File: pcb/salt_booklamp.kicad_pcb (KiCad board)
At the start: 2 copper layers, 45.1 x 45.1 mm, 28 parts, among them J1 USB-C31-S-RA-CS1E-BK-T/R, P1 PIC-TC2050-IDC, U1 PIC16F15213-I/SN, U2 BQ21040DBVR, U3 TPS61158DRVR

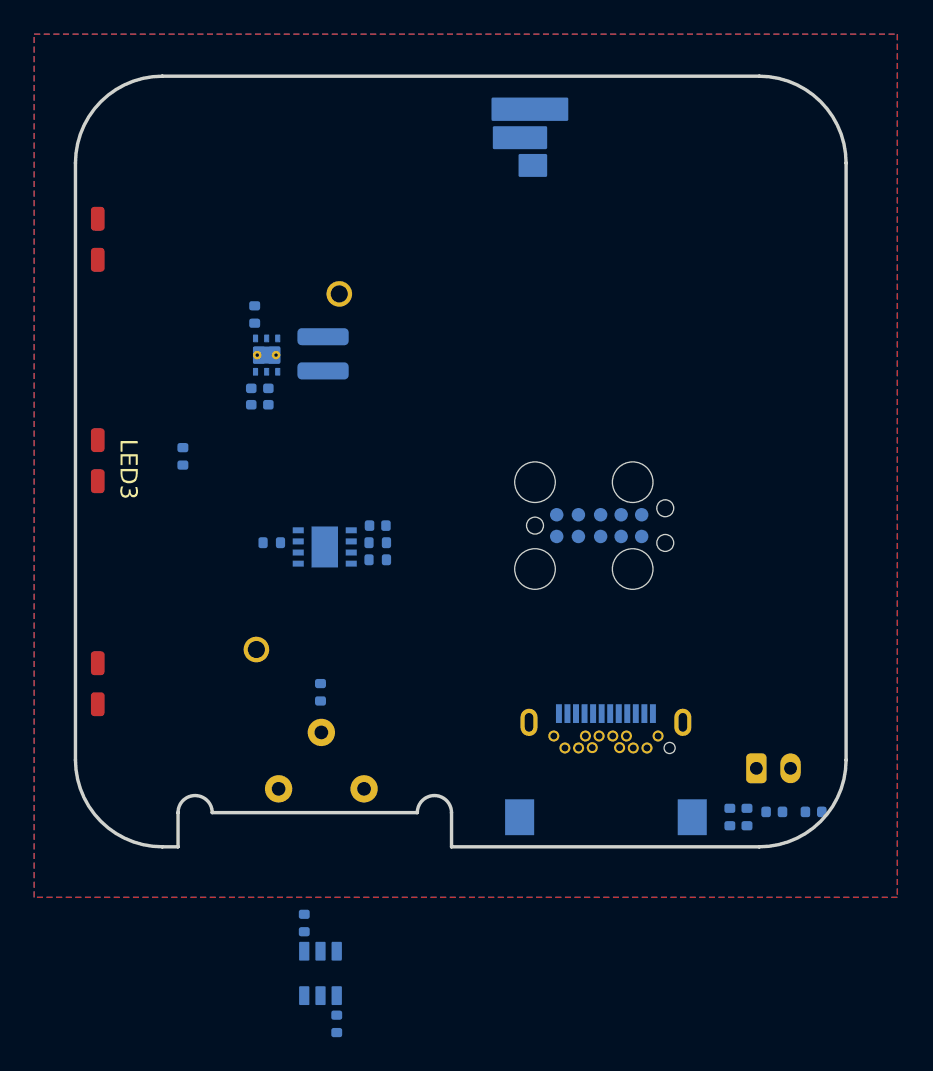
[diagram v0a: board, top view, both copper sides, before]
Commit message: placement work - may need smaller battery connector
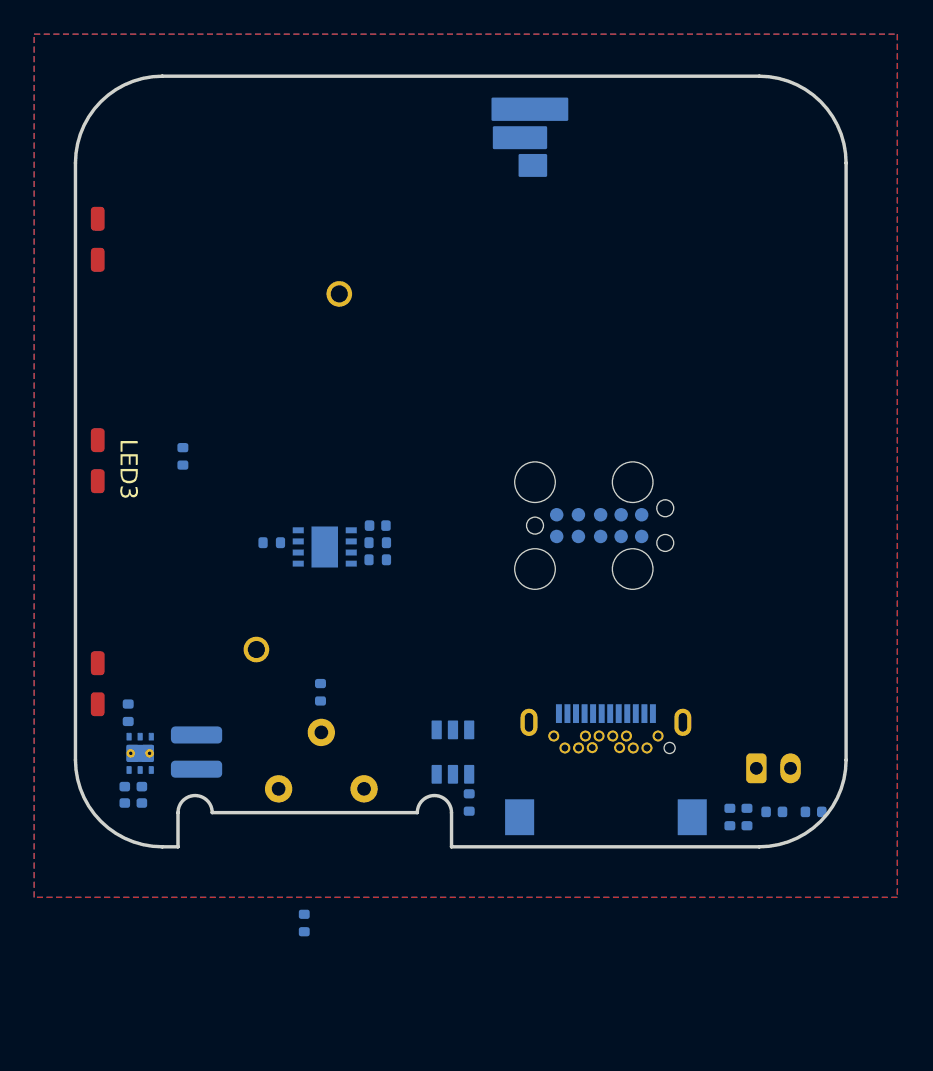
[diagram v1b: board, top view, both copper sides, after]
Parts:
- moved C4 24.4 mm to (204.6, 148.5)
- moved C5 24.4 mm to (205.6, 148.5)
- moved L1 24.4 mm to (208.8, 146.0)
- moved U3 24.4 mm to (205.5, 146.1)
- moved R2 24.4 mm to (204.8, 143.7)
- moved R6 15.1 mm to (224.7, 149.0)
- moved U2 15.1 mm to (223.8, 146.0)
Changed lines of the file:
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@@
 	(footprint "Resistor_SMD:R_0402_1005Metric"
 		(layer "B.Cu")
-		(at 212.182 120.432 -90)
+		(at 204.782 143.732 -90)
 		(descr "Resistor SMD 0402 (1005 Metric), square (rectangular) end terminal, IPC_7351 nominal, (Body size source: IPC-SM-782 page 72, https://www.pcb-3d.com/wordpress/wp-content/uploads/ipc-sm-782a_amendment_1_and_2.pdf), generated with kicad-footprint-generator")
 		(tags "resistor")
@@
 	(footprint "salt_booklamp_footprints:6-WDFN - TPS61158DRVR"
 		(layer "B.Cu")
-		(at 212.882 122.807 90)
+		(at 205.482 146.107 90)
 		(property "Reference" "U3"
 			(at 0 2.1 270)
@@
 	(footprint "salt_booklamp_footprints:BQ21040DBVR"
 		(layer "B.Cu")
-		(at 216.032 158.982)
+		(at 223.782 146.032)
 		(property "Reference" "U2"
 			(at 1.5 3 270)
@@
 	(footprint "Resistor_SMD:R_0402_1005Metric"
 		(layer "B.Cu")
-		(at 216.982 161.932 -90)
+		(at 224.732 148.982 -90)
 		(descr "Resistor SMD 0402 (1005 Metric), square (rectangular) end terminal, IPC_7351 nominal, (Body size source: IPC-SM-782 page 72, https://www.pcb-3d.com/wordpress/wp-content/uploads/ipc-sm-782a_amendment_1_and_2.pdf), generated with kicad-footprint-generator")
 		(tags "resistor")
@@
 	(footprint "salt_booklamp_footprints:ind_VLS3012CX"
 		(layer "B.Cu")
-		(at 216.182 122.732 90)
+		(at 208.782 146.032 90)
 		(property "Reference" "L1"
 			(at 0.2 2.4 270)
@@
 	(footprint "Capacitor_SMD:C_0402_1005Metric"
 		(layer "B.Cu")
-		(at 211.982 125.232 -90)
+		(at 204.582 148.532 -90)
 		(descr "Capacitor SMD 0402 (1005 Metric), square (rectangular) end terminal, IPC_7351 nominal, (Body size source: IPC-SM-782 page 76, https://www.pcb-3d.com/wordpress/wp-content/uploads/ipc-sm-782a_amendment_1_and_2.pdf), generated with kicad-footprint-generator")
 		(tags "capacitor")
@@
 	(footprint "Capacitor_SMD:C_0402_1005Metric"
 		(layer "B.Cu")
-		(at 212.982 125.232 -90)
+		(at 205.582 148.532 -90)
 		(descr "Capacitor SMD 0402 (1005 Metric), square (rectangular) end terminal, IPC_7351 nominal, (Body size source: IPC-SM-782 page 76, https://www.pcb-3d.com/wordpress/wp-content/uploads/ipc-sm-782a_amendment_1_and_2.pdf), generated with kicad-footprint-generator")
 		(tags "capacitor")

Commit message: initial placement for mechanical design -> redesign light guide for 3 LEDs, improve enclosure fit of PCB etc., evaluate battery connector
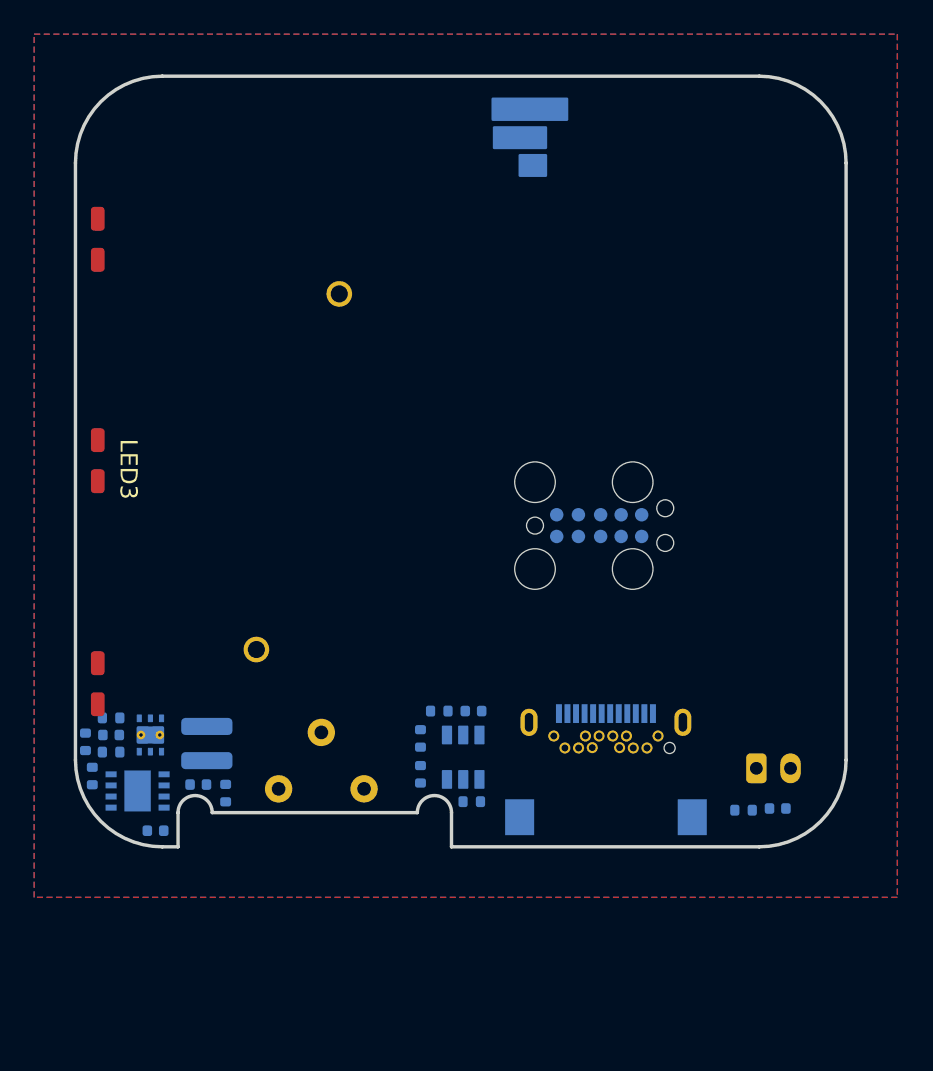
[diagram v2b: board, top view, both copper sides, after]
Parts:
- moved C3 22.1 mm to (206.4, 150.6)
- moved R3 21.6 mm to (202.7, 147.4), turned to 90 degrees
- moved R4 19.2 mm to (203.8, 146.0), turned to 180 degrees
- moved R10 18.7 mm to (221.9, 145.2)
- moved C1 18.6 mm to (225.0, 143.6)
- moved U1 18.0 mm to (205.3, 148.3), turned to 0 degrees
- moved R8 17.6 mm to (202.3, 145.4)
- moved R5 14.9 mm to (210.5, 148.4), turned to 90 degrees
- moved R1 14.7 mm to (223.0, 143.6), turned to 0 degrees
- moved R7 7.57 mm to (221.9, 147.3)
- moved C4 3.59 mm to (203.8, 145.0), turned to 180 degrees
- moved C5 3.35 mm to (208.9, 147.9), turned to 180 degrees
- moved C2 2.11 mm to (242.8, 149.3)
- moved U3 1.23 mm to (206.1, 145.0)
- moved R2 1.04 mm to (203.8, 144.0), turned to 0 degrees
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
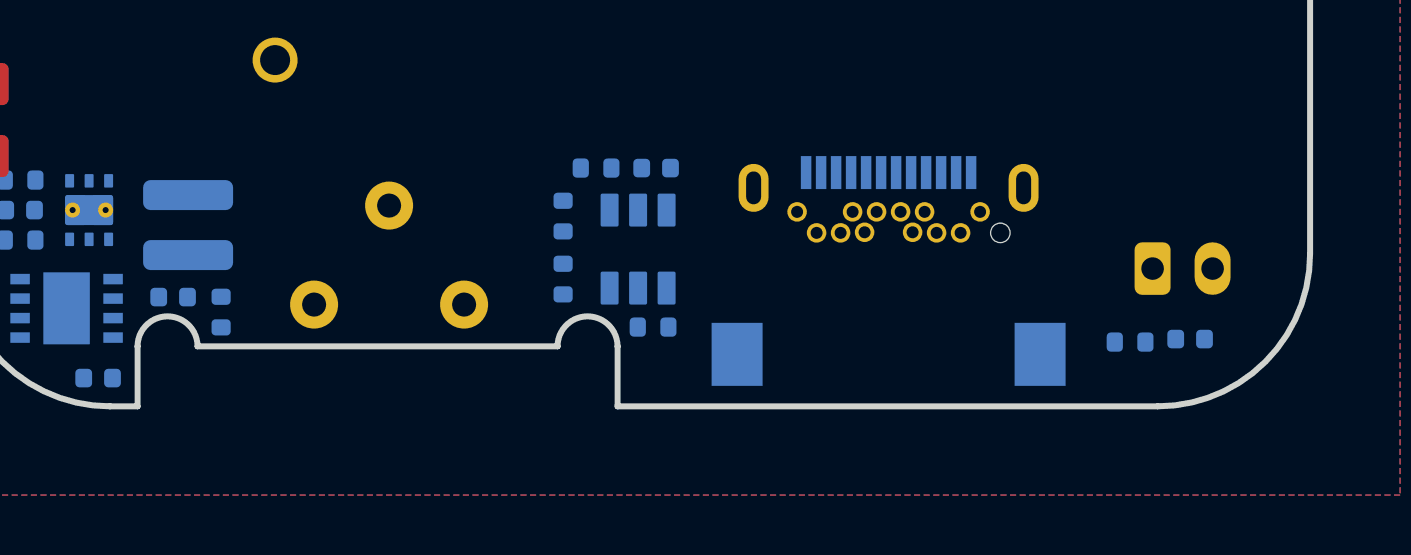
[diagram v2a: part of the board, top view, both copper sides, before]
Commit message: adjust net classes and start routing
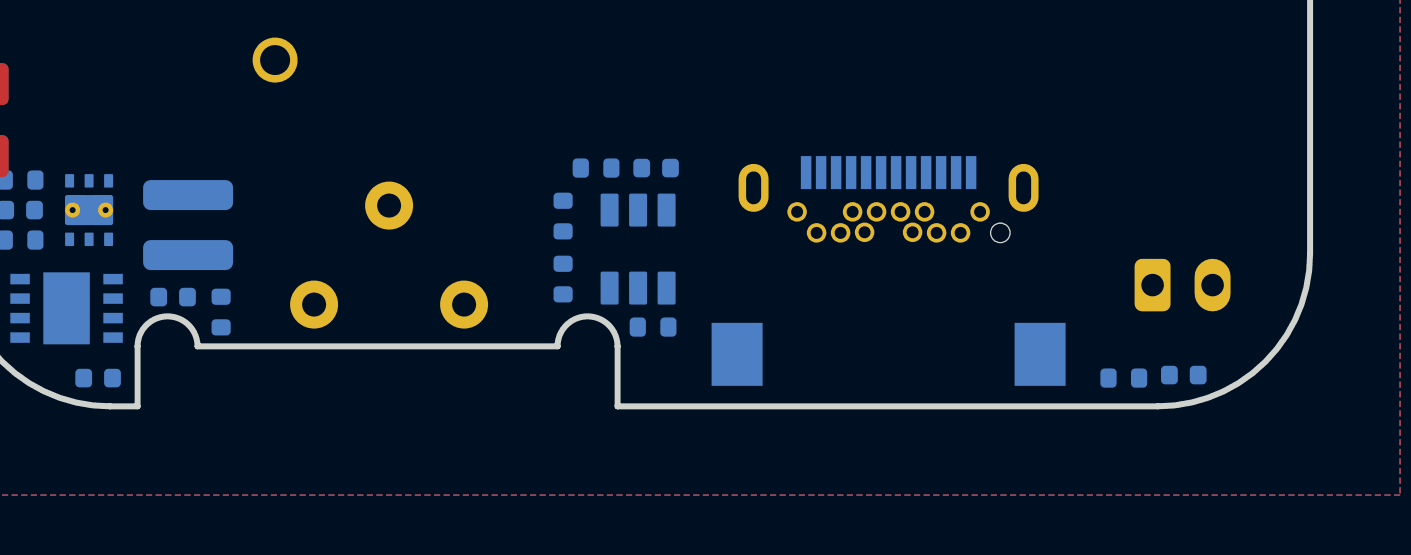
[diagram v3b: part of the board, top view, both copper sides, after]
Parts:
- U1: value PIC16F15213-I/SN -> PIC16F15213T-I/MF
- moved C2 1.22 mm to (242.6, 150.5)
- moved R9 1.22 mm to (240.6, 150.6)
- moved BATT1 0.55 mm to (241.5, 147.5)
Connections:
- net Net-(U3-LX) renamed /LED_DRV_SW
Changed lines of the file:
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@@
 	(net 13 "unconnected-(S1-Pad3)")
 	(net 14 "GND")
-	(net 15 "Net-(U3-LX)")
+	(net 15 "/LED_DRV_SW")
 	(net 16 "unconnected-(J1-SSTSp1-PadA2)")
 	(net 17 "unconnected-(J1-SSTXn1-PadA3)")
@@
 	(footprint "Capacitor_SMD:C_0402_1005Metric"
 		(layer "B.Cu")
-		(at 242.782 149.332 180)
+		(at 242.572 150.532 180)
 		(descr "Capacitor SMD 0402 (1005 Metric), square (rectangular) end terminal, IPC_7351 nominal, (Body size source: IPC-SM-782 page 76, https://www.pcb-3d.com/wordpress/wp-content/uploads/ipc-sm-782a_amendment_1_and_2.pdf), generated with kicad-footprint-generator")
 		(tags "capacitor")
@@
 			(layers "B.Cu" "B.Mask" "B.Paste")
 			(roundrect_rratio 0.1)
-			(net 15 "Net-(U3-LX)")
+			(net 15 "/LED_DRV_SW")
 			(pinfunction "LX")
 			(pintype "passive")
@@
 			)
 		)
-		(property "Value" "PIC16F15213-I/SN"
+		(property "Value" "PIC16F15213T-I/MF"
 			(at 0 -2.55 0)
 			(layer "B.Fab")
@@
 			)
 		)
-		(property "Description" "PIC PIC® 16F, Functional Safety (FuSa) Microcontroller IC 8-Bit 32MHz 3.5KB (2K x 14) FLASH 8-SOIC"
+		(property "Description" "PIC PIC® 16F, Functional Safety (FuSa) Microcontroller IC 8-Bit 32MHz 3.5KB (2K x 14) FLASH 8-DFN (3x3)"
 			(at 0 0 180)
 			(unlocked yes)
@@
 			(layers "B.Cu" "B.Mask" "B.Paste")
 			(roundrect_rratio 0.25)
-			(net 15 "Net-(U3-LX)")
+			(net 15 "/LED_DRV_SW")
 			(pinfunction "2")
 			(pintype "passive")
@@
 	(footprint "GymTimer:JST_PH_S2B-PH-K_1x02_P2.00mm_Horizontal"
 		(layer "B.Cu")
-		(at 241.532 146.982)
+		(at 241.532 147.532)
 		(descr "JST PH series connector, S2B-PH-K (http://www.jst-mfg.com/product/pdf/eng/ePH.pdf), generated with kicad-footprint-generator")
 		(tags "connector JST PH top entry")
@@
 	(footprint "Resistor_SMD:R_0402_1005Metric"
 		(layer "B.Cu")
-		(at 240.782 149.432)
+		(at 240.572 150.632)
 		(descr "Resistor SMD 0402 (1005 Metric), square (rectangular) end terminal, IPC_7351 nominal, (Body size source: IPC-SM-782 page 72, https://www.pcb-3d.com/wordpress/wp-content/uploads/ipc-sm-782a_amendment_1_and_2.pdf), generated with kicad-footprint-generator")
 		(tags "resistor")
@@
 		)
 	)
+	(segment
+		(start 209.362 146.552)
+		(end 209.382 146.532)
+		(width 0.5)
+		(layer "B.Cu")
+		(net 1)
+	)
 	(zone

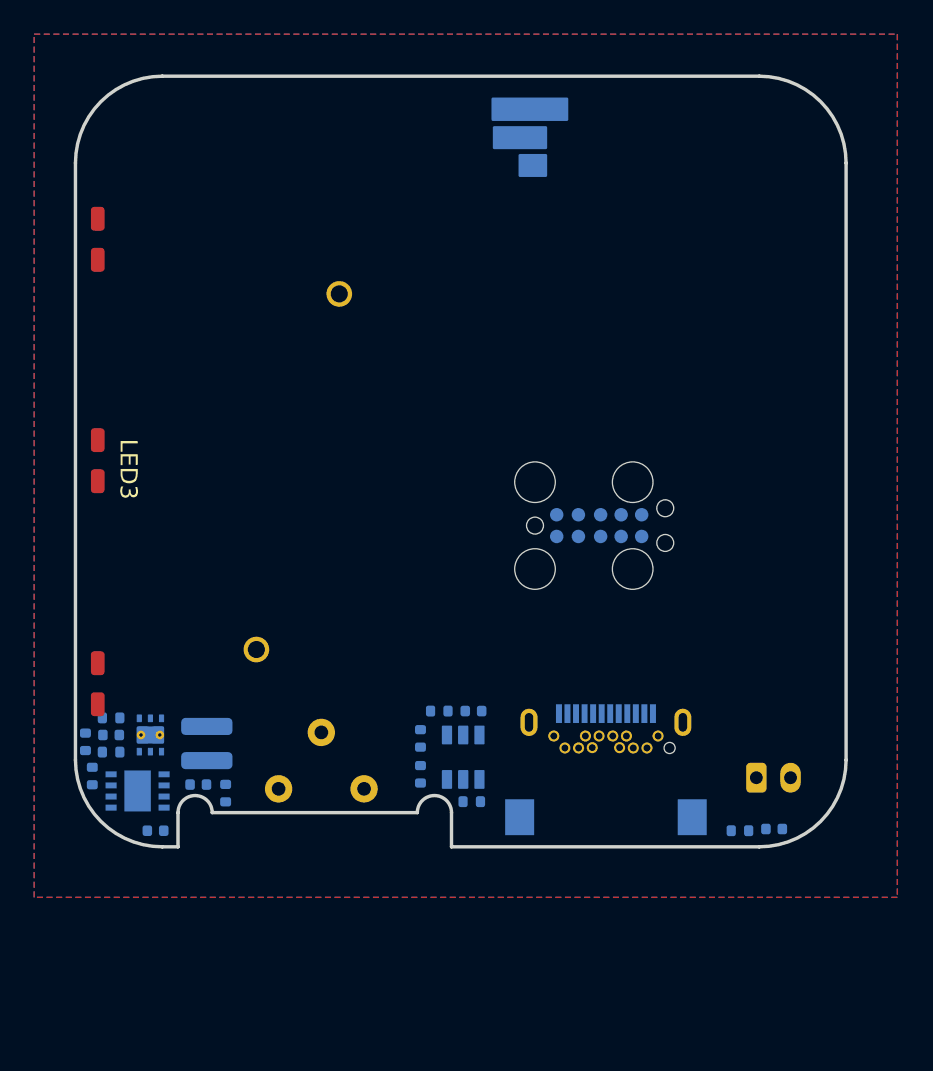
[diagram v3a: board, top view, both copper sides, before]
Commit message: add test point and clean up schematic
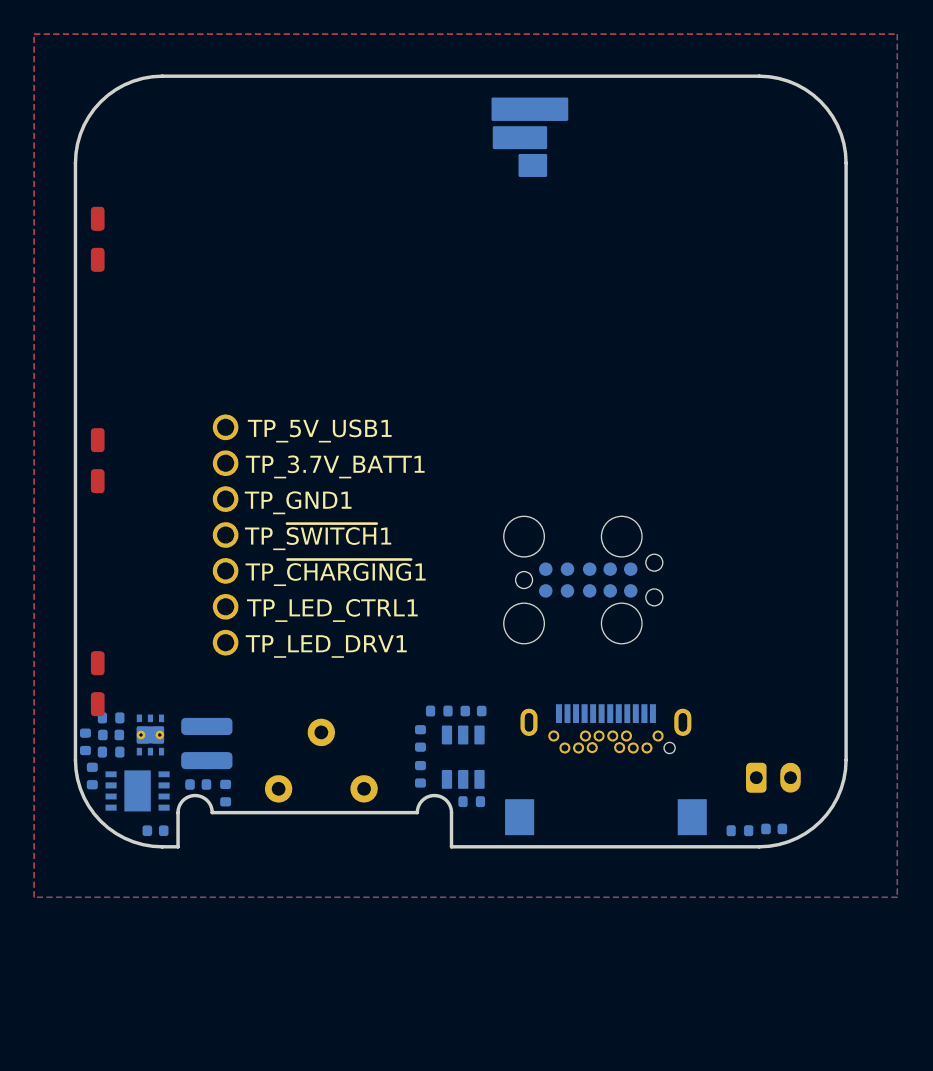
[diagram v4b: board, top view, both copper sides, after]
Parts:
- removed ~{TP_CHG}1: ~, salt_booklamp_footprints:1-pin header
- added TP_3.7V_BATT1: ~, salt_booklamp_footprints:1-pin header, F.Cu at (210.5, 129.1)
- added TP_5V_USB1: ~, salt_booklamp_footprints:1-pin header, F.Cu at (210.5, 127.0)
- added TP_GND1: ~, salt_booklamp_footprints:1-pin header, F.Cu at (210.5, 131.2)
- added TP_LED_CTRL1: ~, salt_booklamp_footprints:1-pin header, F.Cu at (210.5, 137.5)
- added TP_~{CHARGING}1: ~, salt_booklamp_footprints:1-pin header, F.Cu at (210.5, 135.4)
- added TP_~{SWITCH}1: ~, salt_booklamp_footprints:1-pin header, F.Cu at (210.5, 133.3)
- TP_LED_DRV1: moved to F.Cu
- moved TP_LED_DRV1 21.5 mm to (210.5, 139.6)
- moved P1 3.25 mm to (227.9, 136.0)
